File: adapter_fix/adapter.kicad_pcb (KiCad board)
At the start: 2 copper layers, 96 x 18 mm, 10 parts, among them J11 MALE, J12 FEMALE, J13 MALE, J14 STANDOFF, J15 STANDOFF, J16 STANDOFF

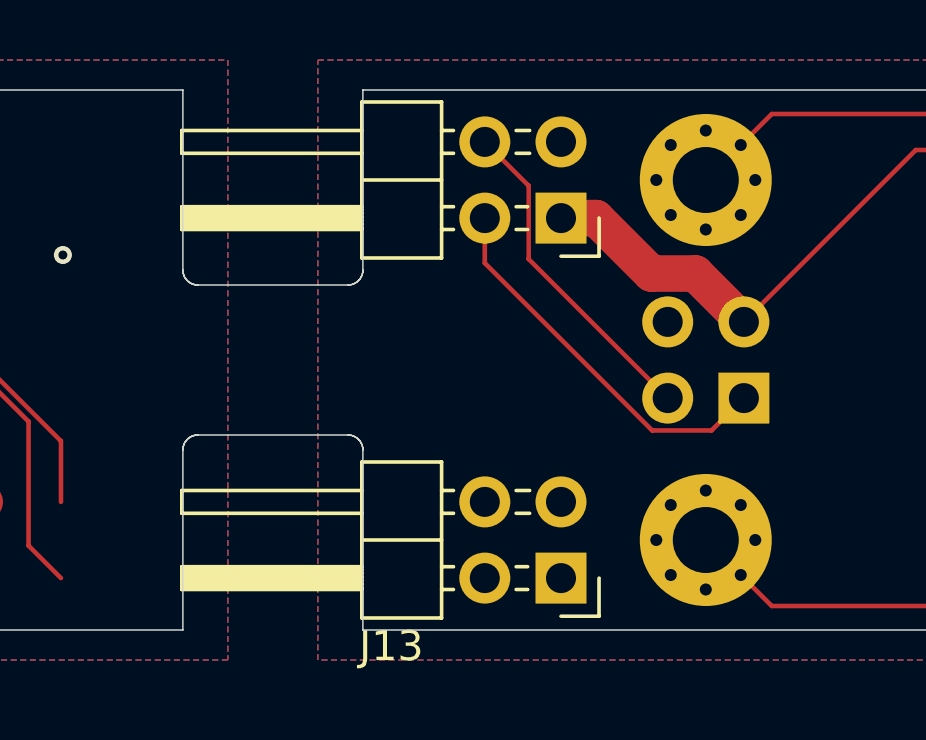
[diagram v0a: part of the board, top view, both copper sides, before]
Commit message: Change footprint(s)
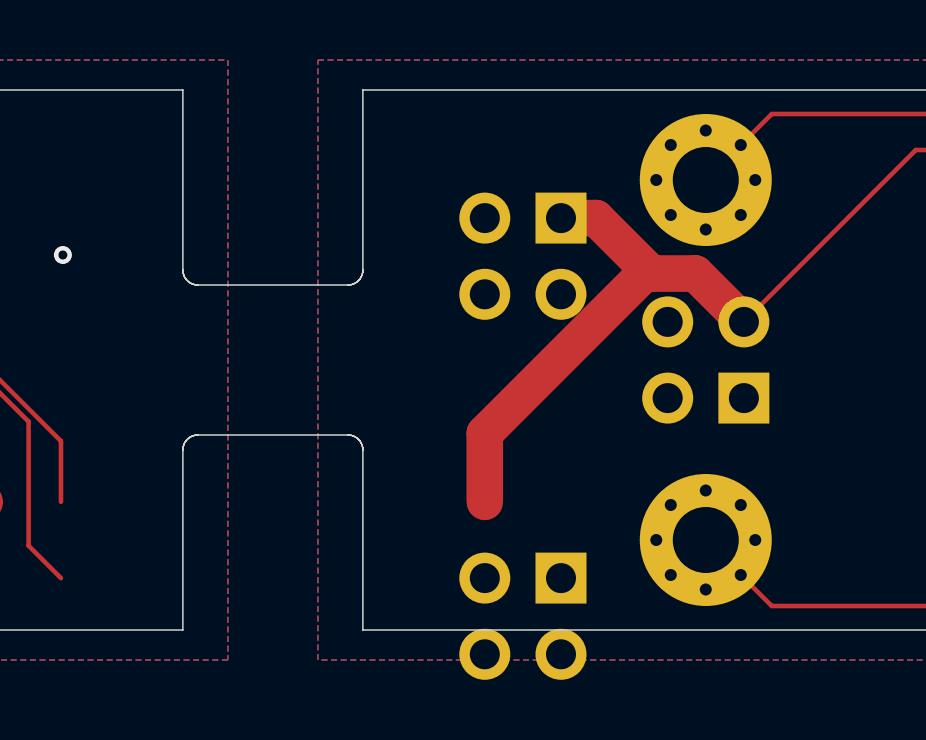
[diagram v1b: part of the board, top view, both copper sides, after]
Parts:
- J11, J13: moved to B.Cu
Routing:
- net Net-(J11-Pad2): track 12.9 -> 0.00 mm
- net Net-(J11-Pad4): track 11.1 -> 0.00 mm
- net +5V: track 47.9 -> 58.0 mm

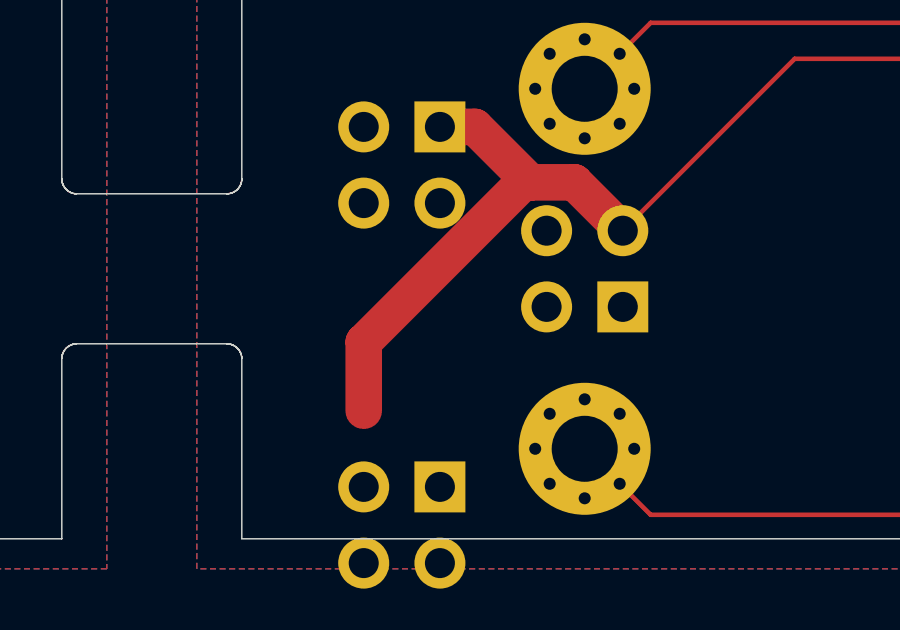
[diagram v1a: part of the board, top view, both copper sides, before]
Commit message: Update footprints
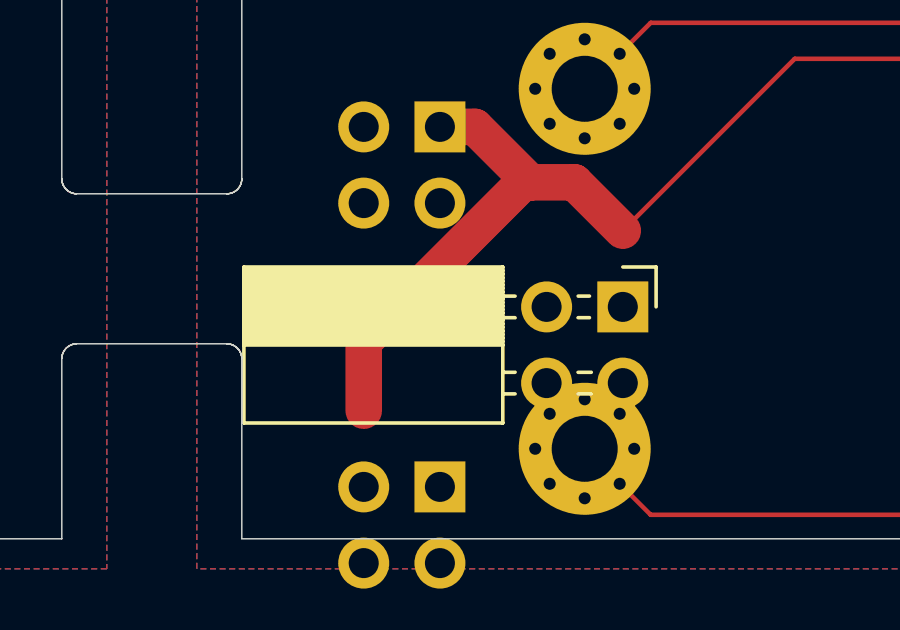
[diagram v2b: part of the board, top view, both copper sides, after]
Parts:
- J12: moved to F.Cu
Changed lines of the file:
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@@
     )
   )
-  (module Connector_PinSocket_2.54mm:PinSocket_2x02_P2.54mm_Horizontal (layer B.Cu)
+  (module Connector_PinSocket_2.54mm:PinSocket_2x02_P2.54mm_Horizontal (layer F.Cu)
     (at 164.2 106.27)
     (descr "Through hole angled socket strip, 2x02, 2.54mm pitch, 8.51mm socket length, double cols (from Kicad 4.0.7), script generated")
     (tags "Through hole angled socket strip THT 2x02 2.54mm double row")
-    (fp_text reference J12 (at -5.65 2.77) (layer B.SilkS) hide
-      (effects (font (size 1 1) (thickness 0.15)) (justify mirror))
+    (fp_text reference J12 (at -5.65 -2.77) (layer F.SilkS) hide
+      (effects (font (size 1 1) (thickness 0.15)))
     )
-    (fp_text value FEMALE (at -5.65 -5.31) (layer B.Fab) hide
-      (effects (font (size 1 1) (thickness 0.15)) (justify mirror))
+    (fp_text value FEMALE (at -5.65 5.31) (layer F.Fab) hide
+      (effects (font (size 1 1) (thickness 0.15)))
     )
-    (fp_line (start 1.8 -4.35) (end 1.8 1.75) (layer B.CrtYd) (width 0.05))
-    (fp_line (start -13.05 -4.35) (end 1.8 -4.35) (layer B.CrtYd) (width 0.05))
-    (fp_line (start -13.05 1.75) (end -13.05 -4.35) (layer B.CrtYd) (width 0.05))
-    (fp_line (start 1.8 1.75) (end -13.05 1.75) (layer B.CrtYd) (width 0.05))
-    (fp_line (start 0 1.33) (end 1.11 1.33) (layer B.SilkS) (width 0.12))
-    (fp_line (start 1.11 1.33) (end 1.11 0) (layer B.SilkS) (width 0.12))
-    (fp_line (start -12.63 1.33) (end -12.63 -3.87) (layer B.SilkS) (width 0.12))
-    (fp_line (start -12.63 -3.87) (end -4 -3.87) (layer B.SilkS) (width 0.12))
-    (fp_line (start -4 1.33) (end -4 -3.87) (layer B.SilkS) (width 0.12))
-    (fp_line (start -12.63 1.33) (end -4 1.33) (layer B.SilkS) (width 0.12))
-    (fp_line (start -12.63 -1.27) (end -4 -1.27) (layer B.SilkS) (width 0.12))
-    (fp_line (start -1.49 -2.9) (end -1.05 -2.9) (layer B.SilkS) (width 0.12))
-    (fp_line (start -4 -2.9) (end -3.59 -2.9) (layer B.SilkS) (width 0.12))
-    (fp_line (start -1.49 -2.18) (end -1.05 -2.18) (layer B.SilkS) (width 0.12))
-    (fp_line (start -4 -2.18) (end -3.59 -2.18) (layer B.SilkS) (width 0.12))
-    (fp_line (start -1.49 -0.36) (end -1.11 -0.36) (layer B.SilkS) (width 0.12))
-    (fp_line (start -4 -0.36) (end -3.59 -0.36) (layer B.SilkS) (width 0.12))
-    (fp_line (start -1.49 0.36) (end -1.11 0.36) (layer B.SilkS) (width 0.12))
-    (fp_line (start -4 0.36) (end -3.59 0.36) (layer B.SilkS) (width 0.12))
-    (fp_line (start -12.63 -1.1519) (end -4 -1.1519) (layer B.SilkS) (width 0.12))
-    (fp_line (start -12.63 -1.033805) (end -4 -1.033805) (layer B.SilkS) (width 0.12))
-    (fp_line (start -12.63 -0.91571) (end -4 -0.91571) (layer B.SilkS) (width 0.12))
-    (fp_line (start -12.63 -0.797615) (end -4 -0.797615) (layer B.SilkS) (width 0.12))
-    (fp_line (start -12.63 -0.67952) (end -4 -0.67952) (layer B.SilkS) (width 0.12))
-    (fp_line (start -12.63 -0.561425) (end -4 -0.561425) (layer B.SilkS) (width 0.12))
-    (fp_line (start -12.63 -0.44333) (end -4 -0.44333) (layer B.SilkS) (width 0.12))
-    (fp_line (start -12.63 -0.325235) (end -4 -0.325235) (layer B.SilkS) (width 0.12))
-    (fp_line (start -12.63 -0.20714) (end -4 -0.20714) (layer B.SilkS) (width 0.12))
-    (fp_line (start -12.63 -0.089045) (end -4 -0.089045) (layer B.SilkS) (width 0.12))
-    (fp_line (start -12.63 0.02905) (end -4 0.02905) (layer B.SilkS) (width 0.12))
-    (fp_line (start -12.63 0.147145) (end -4 0.147145) (layer B.SilkS) (width 0.12))
-    (fp_line (start -12.63 0.26524) (end -4 0.26524) (layer B.SilkS) (width 0.12))
-    (fp_line (start -12.63 0.383335) (end -4 0.383335) (layer B.SilkS) (width 0.12))
-    (fp_line (start -12.63 0.50143) (end -4 0.50143) (layer B.SilkS) (width 0.12))
-    (fp_line (start -12.63 0.619525) (end -4 0.619525) (layer B.SilkS) (width 0.12))
-    (fp_line (start -12.63 0.73762) (end -4 0.73762) (layer B.SilkS) (width 0.12))
-    (fp_line (start -12.63 0.855715) (end -4 0.855715) (layer B.SilkS) (width 0.12))
-    (fp_line (start -12.63 0.97381) (end -4 0.97381) (layer B.SilkS) (width 0.12))
-    (fp_line (start -12.63 1.091905) (end -4 1.091905) (layer B.SilkS) (width 0.12))
-    (fp_line (start -12.63 1.21) (end -4 1.21) (layer B.SilkS) (width 0.12))
-    (fp_line (start 0 -2.84) (end 0 -2.24) (layer B.Fab) (width 0.1))
-    (fp_line (start -4.06 -2.84) (end 0 -2.84) (layer B.Fab) (width 0.1))
-    (fp_line (start 0 -2.24) (end -4.06 -2.24) (layer B.Fab) (width 0.1))
-    (fp_line (start 0 -0.3) (end 0 0.3) (layer B.Fab) (width 0.1))
-    (fp_line (start -4.06 -0.3) (end 0 -0.3) (layer B.Fab) (width 0.1))
-    (fp_line (start 0 0.3) (end -4.06 0.3) (layer B.Fab) (width 0.1))
-    (fp_line (start -12.57 -3.81) (end -12.57 1.27) (layer B.Fab) (width 0.1))
-    (fp_line (start -4.06 -3.81) (end -12.57 -3.81) (layer B.Fab) (width 0.1))
-    (fp_line (start -4.06 0.3) (end -4.06 -3.81) (layer B.Fab) (width 0.1))
-    (fp_line (start -5.03 1.27) (end -4.06 0.3) (layer B.Fab) (width 0.1))
-    (fp_line (start -12.57 1.27) (end -5.03 1.27) (layer B.Fab) (width 0.1))
-    (fp_text user %R (at -8.315 -1.27) (layer B.Fab)
-      (effects (font (size 1 1) (thickness 0.15)) (justify mirror))
+    (fp_line (start 1.8 4.35) (end 1.8 -1.75) (layer F.CrtYd) (width 0.05))
+    (fp_line (start -13.05 4.35) (end 1.8 4.35) (layer F.CrtYd) (width 0.05))
+    (fp_line (start -13.05 -1.75) (end -13.05 4.35) (layer F.CrtYd) (width 0.05))
+    (fp_line (start 1.8 -1.75) (end -13.05 -1.75) (layer F.CrtYd) (width 0.05))
+    (fp_line (start 0 -1.33) (end 1.11 -1.33) (layer F.SilkS) (width 0.12))
+    (fp_line (start 1.11 -1.33) (end 1.11 0) (layer F.SilkS) (width 0.12))
+    (fp_line (start -12.63 -1.33) (end -12.63 3.87) (layer F.SilkS) (width 0.12))
+    (fp_line (start -12.63 3.87) (end -4 3.87) (layer F.SilkS) (width 0.12))
+    (fp_line (start -4 -1.33) (end -4 3.87) (layer F.SilkS) (width 0.12))
+    (fp_line (start -12.63 -1.33) (end -4 -1.33) (layer F.SilkS) (width 0.12))
+    (fp_line (start -12.63 1.27) (end -4 1.27) (layer F.SilkS) (width 0.12))
+    (fp_line (start -1.49 2.9) (end -1.05 2.9) (layer F.SilkS) (width 0.12))
+    (fp_line (start -4 2.9) (end -3.59 2.9) (layer F.SilkS) (width 0.12))
+    (fp_line (start -1.49 2.18) (end -1.05 2.18) (layer F.SilkS) (width 0.12))
+    (fp_line (start -4 2.18) (end -3.59 2.18) (layer F.SilkS) (width 0.12))
+    (fp_line (start -1.49 0.36) (end -1.11 0.36) (layer F.SilkS) (width 0.12))
+    (fp_line (start -4 0.36) (end -3.59 0.36) (layer F.SilkS) (width 0.12))
+    (fp_line (start -1.49 -0.36) (end -1.11 -0.36) (layer F.SilkS) (width 0.12))
+    (fp_line (start -4 -0.36) (end -3.59 -0.36) (layer F.SilkS) (width 0.12))
+    (fp_line (start -12.63 1.1519) (end -4 1.1519) (layer F.SilkS) (width 0.12))
+    (fp_line (start -12.63 1.033805) (end -4 1.033805) (layer F.SilkS) (width 0.12))
+    (fp_line (start -12.63 0.91571) (end -4 0.91571) (layer F.SilkS) (width 0.12))
+    (fp_line (start -12.63 0.797615) (end -4 0.797615) (layer F.SilkS) (width 0.12))
+    (fp_line (start -12.63 0.67952) (end -4 0.67952) (layer F.SilkS) (width 0.12))
+    (fp_line (start -12.63 0.561425) (end -4 0.561425) (layer F.SilkS) (width 0.12))
+    (fp_line (start -12.63 0.44333) (end -4 0.44333) (layer F.SilkS) (width 0.12))
+    (fp_line (start -12.63 0.325235) (end -4 0.325235) (layer F.SilkS) (width 0.12))
+    (fp_line (start -12.63 0.20714) (end -4 0.20714) (layer F.SilkS) (width 0.12))
+    (fp_line (start -12.63 0.089045) (end -4 0.089045) (layer F.SilkS) (width 0.12))
+    (fp_line (start -12.63 -0.02905) (end -4 -0.02905) (layer F.SilkS) (width 0.12))
+    (fp_line (start -12.63 -0.147145) (end -4 -0.147145) (layer F.SilkS) (width 0.12))
+    (fp_line (start -12.63 -0.26524) (end -4 -0.26524) (layer F.SilkS) (width 0.12))
+    (fp_line (start -12.63 -0.383335) (end -4 -0.383335) (layer F.SilkS) (width 0.12))
+    (fp_line (start -12.63 -0.50143) (end -4 -0.50143) (layer F.SilkS) (width 0.12))
+    (fp_line (start -12.63 -0.619525) (end -4 -0.619525) (layer F.SilkS) (width 0.12))
+    (fp_line (start -12.63 -0.73762) (end -4 -0.73762) (layer F.SilkS) (width 0.12))
+    (fp_line (start -12.63 -0.855715) (end -4 -0.855715) (layer F.SilkS) (width 0.12))
+    (fp_line (start -12.63 -0.97381) (end -4 -0.97381) (layer F.SilkS) (width 0.12))
+    (fp_line (start -12.63 -1.091905) (end -4 -1.091905) (layer F.SilkS) (width 0.12))
+    (fp_line (start -12.63 -1.21) (end -4 -1.21) (layer F.SilkS) (width 0.12))
+    (fp_line (start 0 2.84) (end 0 2.24) (layer F.Fab) (width 0.1))
+    (fp_line (start -4.06 2.84) (end 0 2.84) (layer F.Fab) (width 0.1))
+    (fp_line (start 0 2.24) (end -4.06 2.24) (layer F.Fab) (width 0.1))
+    (fp_line (start 0 0.3) (end 0 -0.3) (layer F.Fab) (width 0.1))
+    (fp_line (start -4.06 0.3) (end 0 0.3) (layer F.Fab) (width 0.1))
+    (fp_line (start 0 -0.3) (end -4.06 -0.3) (layer F.Fab) (width 0.1))
+    (fp_line (start -12.57 3.81) (end -12.57 -1.27) (layer F.Fab) (width 0.1))
+    (fp_line (start -4.06 3.81) (end -12.57 3.81) (layer F.Fab) (width 0.1))
+    (fp_line (start -4.06 -0.3) (end -4.06 3.81) (layer F.Fab) (width 0.1))
+    (fp_line (start -5.03 -1.27) (end -4.06 -0.3) (layer F.Fab) (width 0.1))
+    (fp_line (start -12.57 -1.27) (end -5.03 -1.27) (layer F.Fab) (width 0.1))
+    (fp_text user %R (at -8.315 1.27) (layer F.Fab)
+      (effects (font (size 1 1) (thickness 0.15)))
     )
-    (pad 4 thru_hole oval (at -2.54 -2.54) (size 1.7 1.7) (drill 1) (layers *.Cu *.Mask)
+    (pad 4 thru_hole oval (at -2.54 2.54) (size 1.7 1.7) (drill 1) (layers *.Cu *.Mask)
       (net 2 GND))
-    (pad 3 thru_hole oval (at 0 -2.54) (size 1.7 1.7) (drill 1) (layers *.Cu *.Mask)
+    (pad 3 thru_hole oval (at 0 2.54) (size 1.7 1.7) (drill 1) (layers *.Cu *.Mask)
       (net 4 +5V))
     (pad 2 thru_hole oval (at -2.54 0) (size 1.7 1.7) (drill 1) (layers *.Cu *.Mask)

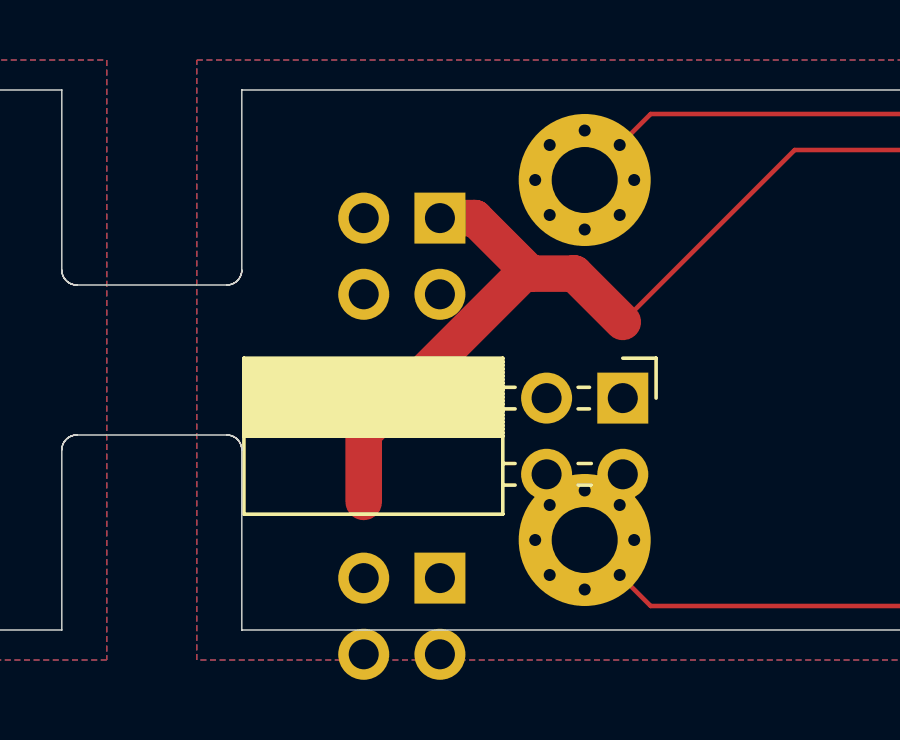
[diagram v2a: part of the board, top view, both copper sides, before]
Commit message: Move footprints to exact positions
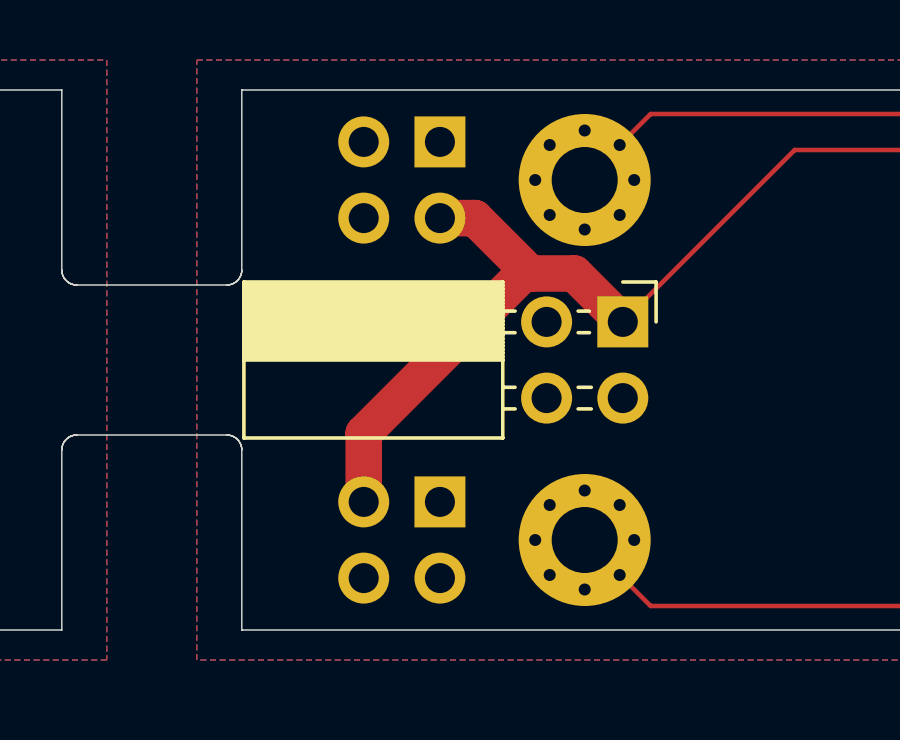
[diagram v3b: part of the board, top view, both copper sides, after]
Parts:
- moved J11 2.54 mm to (158.1, 97.7)
- moved J12 2.54 mm to (164.2, 103.7)
- moved J13 2.54 mm to (158.1, 109.7)
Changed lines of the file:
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@@
   )
   (module Connector_PinHeader_2.54mm:PinHeader_2x02_P2.54mm_Horizontal (layer B.Cu)
-    (at 158.104 100.27 180)
+    (at 158.104 97.73 180)
     (descr "Through hole angled pin header, 2x02, 2.54mm pitch, 6mm pin length, double rows")
     (tags "Through hole angled pin header THT 2x02 2.54mm double row")
@@
   )
   (module Connector_PinSocket_2.54mm:PinSocket_2x02_P2.54mm_Horizontal (layer F.Cu)
-    (at 164.2 106.27)
+    (at 164.2 103.73)
     (descr "Through hole angled socket strip, 2x02, 2.54mm pitch, 8.51mm socket length, double cols (from Kicad 4.0.7), script generated")
     (tags "Through hole angled socket strip THT 2x02 2.54mm double row")
@@
   )
   (module Connector_PinHeader_2.54mm:PinHeader_2x02_P2.54mm_Horizontal (layer B.Cu)
-    (at 158.104 112.27 180)
+    (at 158.104 109.73 180)
     (descr "Through hole angled pin header, 2x02, 2.54mm pitch, 6mm pin length, double rows")
     (tags "Through hole angled pin header THT 2x02 2.54mm double row")

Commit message: Trace
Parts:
- J11, J13: moved to F.Cu
- J12: moved to B.Cu
- moved J11 14.5 mm to (158.1, 112.3)
- moved J13 9.46 mm to (158.1, 100.3)
- moved J12 2.54 mm to (164.2, 106.3)
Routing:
- net +5VB: track 51.1 -> 0.00 mm
- net /Lower Board/TXD: track 24.1 -> 0.00 mm
- net /Lower Board/RXD: track 22.4 -> 0.00 mm
- net Net-(J11-Pad2): track 0.00 -> 22.2 mm
- net /Lower Board/D-: track 21.6 -> 0.00 mm, vias 2 -> 0
- net /Lower Board/RXLED: track 19.3 -> 0.00 mm, vias 1 -> 0
- net /Lower Board/VBUS: track 19.1 -> 0.00 mm
- net /Lower Board/TXLED: track 18.9 -> 0.00 mm
- net Net-(J6-PadB5): track 18.7 -> 0.00 mm
- net /Lower Board/D+: track 16.9 -> 0.00 mm, vias 2 -> 0
- net Net-(J11-Pad4): track 0.00 -> 15.0 mm
- net GNDB: track 14.4 -> 0.00 mm, vias 8 -> 0
- net +5V: track 58.0 -> 65.5 mm
- net Net-(J6-PadA5): track 7.34 -> 0.00 mm
- net /Lower Board/DTR: track 5.59 -> 0.00 mm
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- removed copper zone on B.Cu, net GNDB
- removed copper zone on F.Cu, net GNDB
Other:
- board size 96 x 18 mm -> 45 x 18 mm
